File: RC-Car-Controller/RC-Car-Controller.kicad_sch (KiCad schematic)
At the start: 4 parts

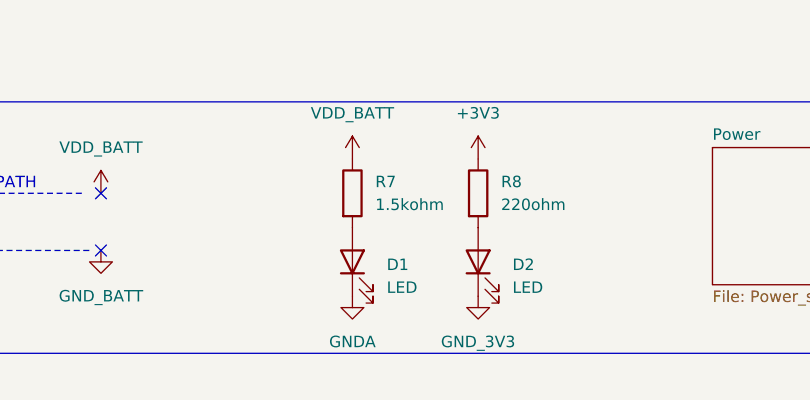
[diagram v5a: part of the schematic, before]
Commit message: Redid USB C Footprint
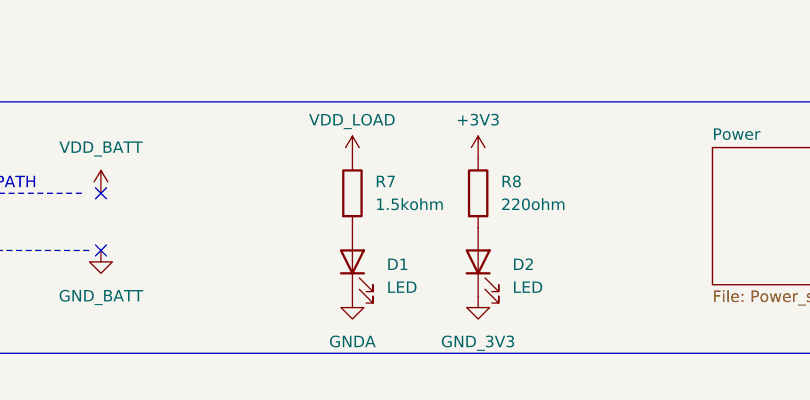
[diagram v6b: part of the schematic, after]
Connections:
- net VDD_BATT: no longer R7.1
- net VDD_LOAD: now also R7.1
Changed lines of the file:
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@@
 		(on_board yes)
 		(dnp no)
-		(fields_autoplaced yes)
 		(property "Reference" "#PWR040"
 			(at 180.34 34.29 0)
@@
 		)
 		(property "Value" "+3V3"
-			(at 180.34 25.4 0)
+			(at 180.34 26.162 0)
 			(effects
 				(font
@@
 		(on_board yes)
 		(dnp no)
-		(fields_autoplaced yes)
 		(property "Reference" "#PWR033"
 			(at 166.37 34.29 0)
@@
 			)
 		)
-		(property "Value" "VDD_BATT"
-			(at 166.37 25.4 0)
-			(effects
-				(font
-					(size 1.27 1.27)
-				)
-			)
-		)
+		(property "Value" "VDD_LOAD"
+			(at 161.544 26.162 0)
+			(effects
+				(font
+					(size 1.27 1.27)
+				)
+				(justify left)
+			)
+		)

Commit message: Did power schtuff
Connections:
- no-connect marks 9 -> 10
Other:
- sheet MCU ports: added I2C3_SCL, I2C3_SDA, SPI1_CS, SPI1_DC, SPI1_MISO, SPI1_MOSI, SPI1_SCLK, SPI4_MISO, SPI4_MOSI, SPI4_SCLK; removed RF_NRST, SPI2_CS_LCD, SPI2_MISO, SPI2_MOSI, SPI2_SCLK, SPI3_CS_ADC, SPI3_MISO, SPI3_MOSI, SPI3_SCLK, SPI4_CS_RF, SPI4_MISO_RF, SPI4_MOSI_RF, SPI4_SCLK_RF
- sheet Power ports: added GAS_SCL, GAS_SDA; removed none
- sheet RF ports: added none; removed CS, IRQ, MISO, MOSI, RF_ANT, RSTN, SCLK

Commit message: Did a bunch of stuff on the controller
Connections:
- no-connect marks 10 -> 9
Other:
- sheet MCU ports: added SDMMC1_CK, SDMMC1_CMD, SDMMC1_D0, SDMMC1_D1, SDMMC1_D2, SDMMC1_D3, SPI4_CS, SPI4_DC; removed I2C3_SCL, I2C3_SDA, SPI4_MISO
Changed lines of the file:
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@@
+		(color 0 0 0 0)
+	)
+	(junction
+		(at 91.44 151.13)
+		(diameter 0)
+		(color 0 0 0 0)
+	)
+	(junction
+		(at 88.9 148.59)
+		(diameter 0)
 		(color 0 0 0 0)
 	)
@@
 	)
 	(no_connect
-		(at 113.03 124.46)
-	)
-	(no_connect
 		(at 165.1 69.85)
 	)
@@
 	(wire
 		(pts
-			(xy 148.59 130.81) (xy 166.37 130.81)
-		)
-		(stroke
-			(width 0)
-			(type default)
-		)
-	)
-	(wire
-		(pts
 			(xy 85.09 140.97) (xy 113.03 140.97)
 		)
@@
 	(wire
 		(pts
-			(xy 85.09 151.13) (xy 113.03 151.13)
+			(xy 85.09 151.13) (xy 91.44 151.13)
+		)
+		(stroke
+			(width 0)
+			(type default)
+		)
+	)
+	(wire
+		(pts
+			(xy 85.09 129.54) (xy 113.03 129.54)
+		)
+		(stroke
+			(width 0)
+			(type default)
+		)
+	)
+	(wire
+		(pts
+			(xy 91.44 151.13) (xy 113.03 151.13)
 		)
 		(stroke
@@
 	(wire
 		(pts
-			(xy 85.09 148.59) (xy 113.03 148.59)
+			(xy 88.9 148.59) (xy 113.03 148.59)
+		)
+		(stroke
+			(width 0)
+			(type default)
+		)
+	)
+	(wire
+		(pts
+			(xy 85.09 148.59) (xy 88.9 148.59)
 		)
 		(stroke
@@
 	(wire
 		(pts
-			(xy 110.49 121.92) (xy 113.03 121.92)
+			(xy 88.9 165.1) (xy 88.9 148.59)
 		)
 		(stroke
@@
 	(wire
 		(pts
+			(xy 85.09 167.64) (xy 91.44 167.64)
+		)
+		(stroke
+			(width 0)
+			(type default)
+		)
+	)
+	(wire
+		(pts
+			(xy 91.44 167.64) (xy 91.44 151.13)
+		)
+		(stroke
+			(width 0)
+			(type default)
+		)
+	)
+	(wire
+		(pts
 			(xy 148.59 95.25) (xy 165.1 95.25)
 		)
@@
 	(wire
 		(pts
-			(xy 148.59 128.27) (xy 166.37 128.27)
-		)
-		(stroke
-			(width 0)
-			(type default)
-		)
-	)
-	(wire
-		(pts
 			(xy 60.96 40.64) (xy 74.93 40.64)
 		)
@@
 	(wire
 		(pts
+			(xy 85.09 132.08) (xy 113.03 132.08)
+		)
+		(stroke
+			(width 0)
+			(type default)
+		)
+	)
+	(wire
+		(pts
 			(xy 148.59 97.79) (xy 165.1 97.79)
 		)
@@
 	(wire
 		(pts
-			(xy 85.09 124.46) (xy 110.49 124.46)
+			(xy 85.09 124.46) (xy 113.03 124.46)
+		)
+		(stroke
+			(width 0)
+			(type default)
+		)
+	)
+	(wire
+		(pts
+			(xy 85.09 165.1) (xy 88.9 165.1)
 		)
 		(stroke
@@
 		(pts
 			(xy 85.09 105.41) (xy 113.03 105.41)
-		)
-		(stroke
-			(width 0)
-			(type default)
-		)
-	)
-	(wire
-		(pts
-			(xy 110.49 124.46) (xy 110.49 121.92)
 		)
 		(stroke
@@
 	)
 	(sheet
-		(at 113.03 82.55)
-		(size 35.56 72.39)
+		(at 113.03 76.2)
+		(size 35.56 78.74)
 		(fields_autoplaced yes)
 		(stroke
@@
 		)
 		(property "Sheetname" "MCU"
-			(at 113.03 81.8384 0)
+			(at 113.03 75.4884 0)
 			(effects
 				(font
@@
 			)
 		)
-		(pin "SPI4_MISO" input
-			(at 113.03 124.46 180)
-			(effects
-				(font
-					(size 1.27 1.27)
-				)
-				(justify left)
-			)
-		)
 		(pin "SPI4_MOSI" input
 			(at 113.03 127 180)
@@
 		)
 		(pin "SPI4_SCLK" input
-			(at 113.03 121.92 180)
+			(at 113.03 124.46 180)
 			(effects
 				(font
@@
 			)
 		)
-		(pin "I2C3_SCL" input
-			(at 148.59 130.81 0)
-			(effects
-				(font
-					(size 1.27 1.27)
-				)
-				(justify right)
-			)
-		)
-		(pin "I2C3_SDA" input
-			(at 148.59 128.27 0)
-			(effects
-				(font
-					(size 1.27 1.27)
-				)
-				(justify right)
+		(pin "SDMMC1_CMD" input
+			(at 113.03 78.74 180)
+			(effects
+				(font
+					(size 1.27 1.27)
+				)
+				(justify left)
+			)
+		)
+		(pin "SDMMC1_D0" input
+			(at 113.03 83.82 180)
+			(effects
+				(font
+					(size 1.27 1.27)
+				)
+				(justify left)
+			)
+		)
+		(pin "SDMMC1_D1" input
+			(at 113.03 86.36 180)
+			(effects
+				(font
+					(size 1.27 1.27)
+				)
+				(justify left)
+			)
+		)
+		(pin "SDMMC1_D2" input
+			(at 113.03 88.9 180)
+			(effects
+				(font
+					(size 1.27 1.27)
+				)
+				(justify left)
+			)
+		)
+		(pin "SDMMC1_CK" input
+			(at 113.03 81.28 180)
+			(effects
+				(font
+					(size 1.27 1.27)
+				)
+				(justify left)
+			)
+		)
+		(pin "SDMMC1_D3" input
+			(at 113.03 91.44 180)
+			(effects
+				(font
+					(size 1.27 1.27)
+				)
+				(justify left)
+			)
+		)
+		(pin "SPI4_CS" input
+			(at 113.03 129.54 180)
+			(effects
+				(font
+					(size 1.27 1.27)
+				)
+				(justify left)
+			)
+		)
+		(pin "SPI4_DC" input
+			(at 113.03 132.08 180)
+			(effects
+				(font
+					(size 1.27 1.27)
+				)
+				(justify left)
 			)
 		)
@@
 	)
 	(sheet
-		(at 165.1 121.92)
-		(size 30.48 15.24)
+		(at 52.07 160.02)
+		(size 33.02 15.24)
 		(fields_autoplaced yes)
 		(stroke
@@
 		)
 		(property "Sheetname" "Power"
-			(at 165.1 121.2084 0)
+			(at 52.07 159.3084 0)
 			(effects
 				(font
@@
 		)
 		(property "Sheetfile" "Power_sch.kicad_sch"
-			(at 165.1 137.7446 0)
+			(at 52.07 175.8446 0)
 			(effects
 				(font
@@
 		)
 		(pin "GAS_SCL" input
-			(at 165.1 130.81 180)
-			(effects
-				(font
-					(size 1.27 1.27)
-				)
-				(justify left)
+			(at 85.09 167.64 0)
+			(effects
+				(font
+					(size 1.27 1.27)
+				)
+				(justify right)
 			)
 		)
 		(pin "GAS_SDA" input
-			(at 165.1 128.27 180)
-			(effects
-				(font
-					(size 1.27 1.27)
-				)
-				(justify left)
-			)
-		)
+			(at 85.09 165.1 0)
+			(effects
+				(font
+					(size 1.27 1.27)
+				)
+				(justify right)
+			)
+		)
